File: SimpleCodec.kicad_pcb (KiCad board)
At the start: 4 copper layers, 115 parts, among them J1 DC-005-2.5A-2.0, J2 NMJ6HCD2, J3 NMJ6HCD2, Q1 AO3401A, U1 AMS1117-5.0, U2 AMS1117-3.3, U3 NE5532, U4 NE5532, U5 NE5532, U6 NE5532, U7 NE5532, U8 CS4272

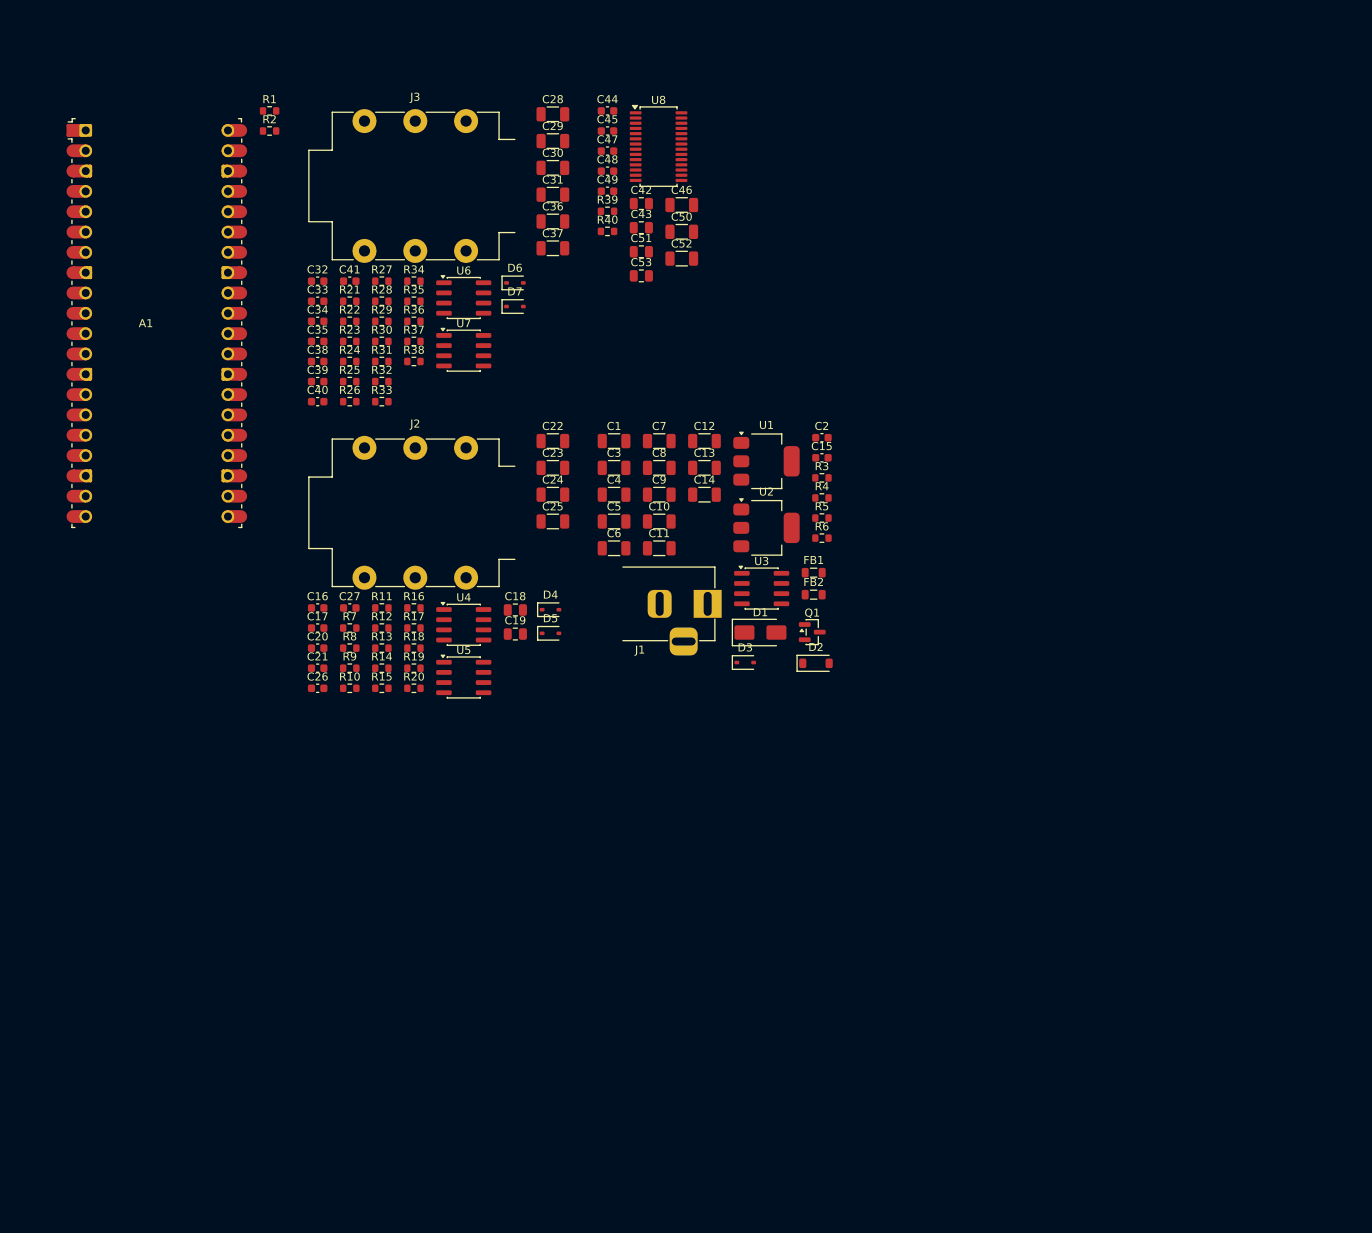
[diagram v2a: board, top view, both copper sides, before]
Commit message: Initial layout
Initial layout inside a 1590N1/125B pedal enclosure.
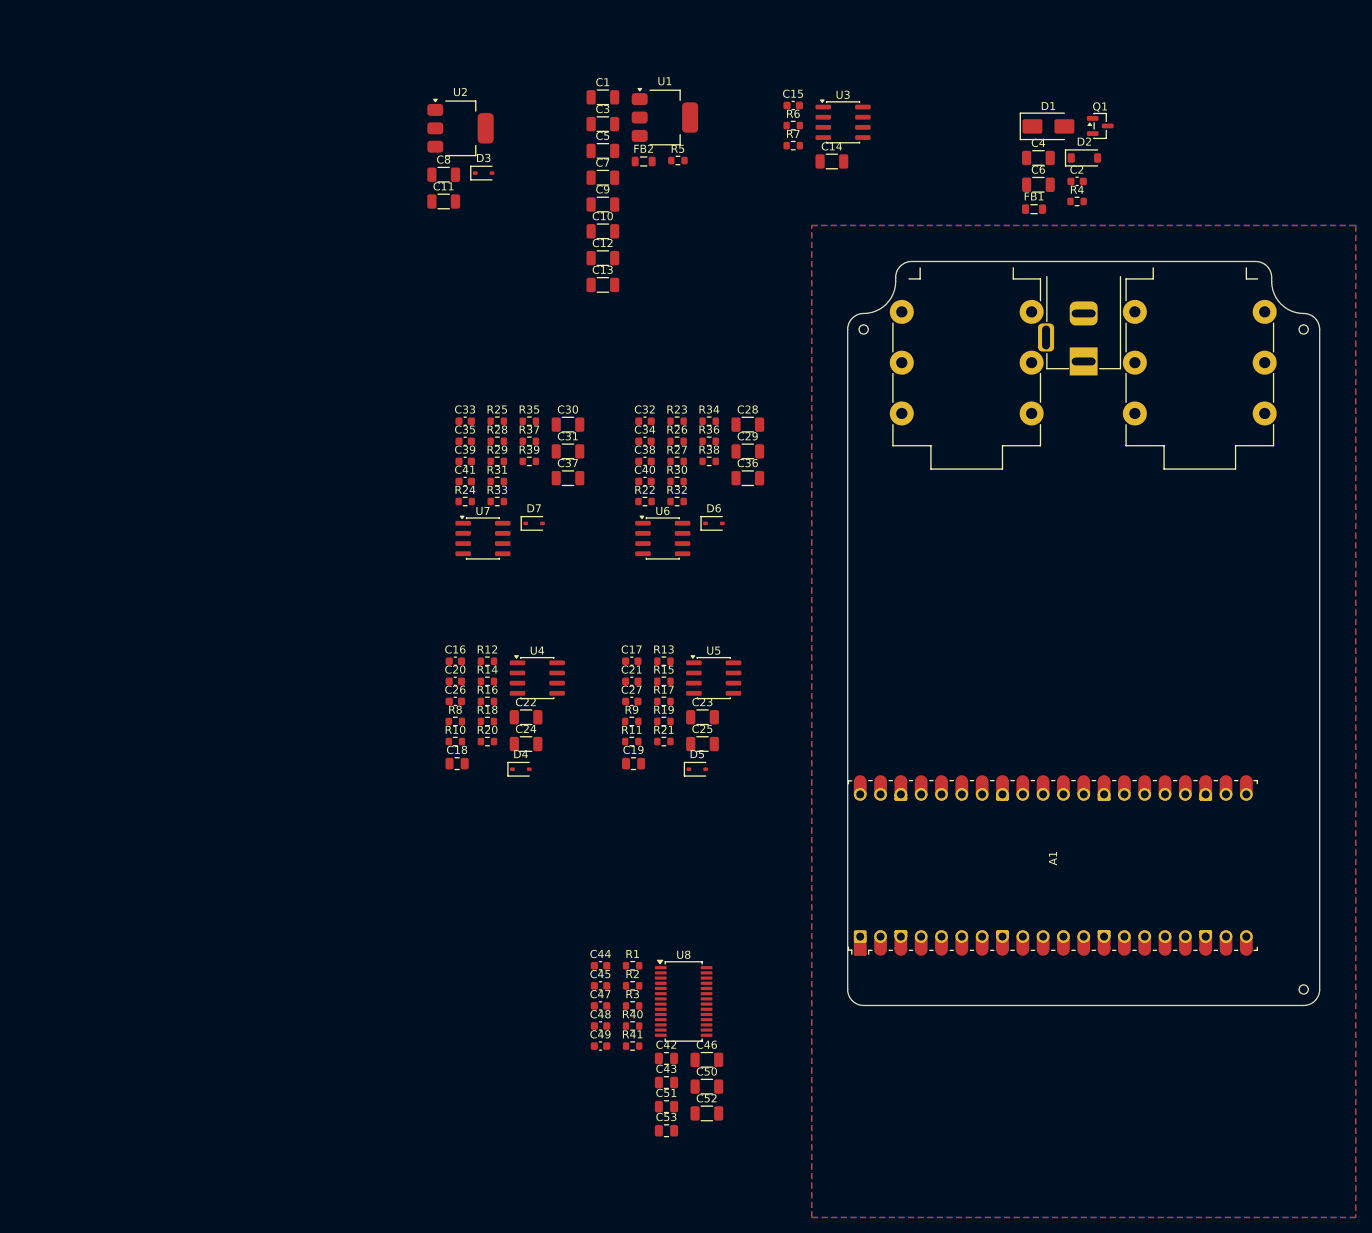
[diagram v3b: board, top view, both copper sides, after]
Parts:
- removed J1: DC-005-2.5A-2.0, Custom_Parts:BARREL_JACK_HORIZONTAL
- removed J2, J3: NMJ6HCD2, Custom_Parts:NMJ6HCD2_BORDER
- added H1: Tooling, MountingHole:ToolingHole_1.152mm, F.Cu at (122.5, 51.0)
- added H2: Tooling, MountingHole:ToolingHole_1.152mm, F.Cu at (177.5, 51.0)
- added H3: Tooling, MountingHole:ToolingHole_1.152mm, F.Cu at (177.5, 133.5)
- added R41: 47K, Resistor_SMD:R_0603_1608Metric, F.Cu at (93.6, 140.6)
- added REF**: Hammond_125B_1590N1_NOLID, Enclosures:Hammond_125B_1590N1_NOLID, B.Cu at (150.0, 100.0)
- added X1: PEDAL_COMBO_TOP, Custom_Parts:PEDAL_COMBO_TOP, F.Cu at (150.0, 44.0)
- R13: value 1K -> 100K
- R17: value 10K -> 1K
- R19: value 1K -> 10K
- R21: value 100K -> 1K
- R25: value 12K -> 100K
- R29: value 22K -> 12K
- R3: value 4.7K -> 47K
- R33: value 220 -> 22K
- R35: value 100 -> 220
- R37: value 47K -> 100
- R4, R7: value 100 -> 4.7K
- R5: value 4.7K -> 100
- R9: value 100K -> 100
- moved A1 130.9 mm to (146.2, 118.0), turned to 90 degrees
- moved R1 116.1 mm to (93.6, 130.5)
- moved R2 116.1 mm to (93.6, 133.0)
- moved C50 106.9 mm to (102.9, 145.6)
- moved C51 106.9 mm to (97.8, 148.1)
- moved C52 106.9 mm to (102.9, 149.0)
- moved C53 106.9 mm to (97.8, 151.2)
- moved U8 106.9 mm to (100.0, 135.0)
- moved C42 106.9 mm to (97.8, 142.1)
- moved C43 106.9 mm to (97.8, 145.1)
- moved C46 106.9 mm to (102.9, 142.3)
- moved C47 106.9 mm to (89.6, 135.6)
- moved C44 106.9 mm to (89.6, 130.5)
- moved C45 106.9 mm to (89.6, 133.0)
- moved C48 106.9 mm to (89.6, 138.1)
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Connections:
- R10 pad 2: Net-(C17-Pad1) -> Net-(C16-Pad1)
- R11 pad 1: Net-(U4A-+) -> GND
- R11 pad 2: +VBIAS_IN -> Net-(C17-Pad1)
- R12 pad 1: Net-(U5A-+) -> Net-(U4A-+)
- R13 pad 1: Net-(U4A--) -> Net-(U5A-+)
- R13 pad 2: Net-(C20-Pad1) -> +VBIAS_IN
- R14 pad 1: Net-(U5A--) -> Net-(U4A--)
- R14 pad 2: Net-(C21-Pad1) -> Net-(C20-Pad1)
- R15 pad 1: GND -> Net-(U5A--)
- R15 pad 2: Net-(C20-Pad1) -> Net-(C21-Pad1)
- R16 pad 2: Net-(C21-Pad1) -> Net-(C20-Pad1)
- R17 pad 1: Net-(U4B-+) -> GND
- R17 pad 2: VBIAS_IN -> Net-(C21-Pad1)
- R18 pad 1: Net-(U5B-+) -> Net-(U4B-+)
- R19 pad 1: Net-(C24-Pad2) -> Net-(U5B-+)
- R19 pad 2: CODEC_INL -> VBIAS_IN
- R20 pad 1: Net-(C25-Pad2) -> Net-(C24-Pad2)
- R20 pad 2: CODEC_INR -> CODEC_INL
- R21 pad 1: +VBIAS_OUT -> Net-(C25-Pad2)
- R21 pad 2: Net-(C28-Pad2) -> CODEC_INR
- R22 pad 1: Net-(C29-Pad2) -> +VBIAS_OUT
- R22 pad 2: VBIAS_OUT -> Net-(C28-Pad2)
- R23 pad 1: +VBIAS_OUT -> Net-(C29-Pad2)
- R23 pad 2: Net-(C30-Pad2) -> VBIAS_OUT
- R24 pad 1: Net-(C31-Pad2) -> +VBIAS_OUT
- R24 pad 2: VBIAS_OUT -> Net-(C30-Pad2)
- R25 pad 1: Net-(C28-Pad2) -> Net-(C31-Pad2)
- R25 pad 2: Net-(U6A--) -> VBIAS_OUT
- R26 pad 1: Net-(C29-Pad2) -> Net-(C28-Pad2)
- R26 pad 2: Net-(U6A-+) -> Net-(U6A--)
- R27 pad 1: Net-(C30-Pad2) -> Net-(C29-Pad2)
- R27 pad 2: Net-(U7A--) -> Net-(U6A-+)
- R28 pad 1: Net-(C31-Pad2) -> Net-(C30-Pad2)
- R28 pad 2: Net-(U7A-+) -> Net-(U7A--)
- R29 pad 1: Net-(U6A-+) -> Net-(C31-Pad2)
- R29 pad 2: VBIAS_OUT -> Net-(U7A-+)
- R3 pad 1: /Power/PROT_G -> CODEC_RST
- R30 pad 1: Net-(U7A-+) -> Net-(U6A-+)
- R31 pad 1: Net-(U6A--) -> Net-(U7A-+)
- R31 pad 2: Net-(C32-Pad2) -> VBIAS_OUT
- R32 pad 1: Net-(U7A--) -> Net-(U6A--)
- R32 pad 2: Net-(C33-Pad2) -> Net-(C32-Pad2)
- R33 pad 1: Net-(C32-Pad2) -> Net-(U7A--)
- R33 pad 2: Net-(U6B-+) -> Net-(C33-Pad2)
- R34 pad 1: Net-(C33-Pad2) -> Net-(C32-Pad2)
- R34 pad 2: Net-(U7B-+) -> Net-(U6B-+)
- R35 pad 1: Net-(C36-Pad2) -> Net-(C33-Pad2)
- R35 pad 2: /Buffers_Out/AUDIO_OUTL -> Net-(U7B-+)
- R36 pad 1: Net-(C37-Pad2) -> Net-(C36-Pad2)
- R36 pad 2: /Buffers_Out/AUDIO_OUTR -> /Buffers_Out/AUDIO_OUTL
- R37 pad 1: /Buffers_Out/AUDIO_OUTL -> Net-(C37-Pad2)
- R37 pad 2: GND -> /Buffers_Out/AUDIO_OUTR
- R38 pad 1: /Buffers_Out/AUDIO_OUTR -> /Buffers_Out/AUDIO_OUTL
- R39 pad 1: Net-(U8-~{BMUTEC}) -> /Buffers_Out/AUDIO_OUTR
- R4 pad 1: +VCC -> /Power/PROT_G
- R4 pad 2: +VCC_FILT -> GND
- R40 pad 1: Net-(U8-~{AMUTEC}) -> Net-(U8-~{BMUTEC})
- R5 pad 1: +VCC_FILT -> +VCC
- R5 pad 2: /Power/+VBIAS_RAW -> +VCC_FILT
- R6 pad 1: /Power/+VBIAS_RAW -> +VCC_FILT
- R6 pad 2: GND -> /Power/+VBIAS_RAW
- R7 pad 1: /Buffers_In/AUDIO_INL -> /Power/+VBIAS_RAW
- R7 pad 2: Net-(C16-Pad1) -> GND
- R8 pad 1: /Buffers_In/AUDIO_INR -> /Buffers_In/AUDIO_INL
- R8 pad 2: Net-(C17-Pad1) -> Net-(C16-Pad1)
- R9 pad 1: GND -> /Buffers_In/AUDIO_INR
- R9 pad 2: Net-(C16-Pad1) -> Net-(C17-Pad1)
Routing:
- added copper zone on B.Cu, net GND
- added copper zone on F.Cu, net GND
- added copper zone on In1.Cu, net GND
- added copper zone on In2.Cu, net GND
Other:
- board outline added: 59 x 93 mm

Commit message: RP2350 layout
Updated the layout for the RP2350.
Added board headers.
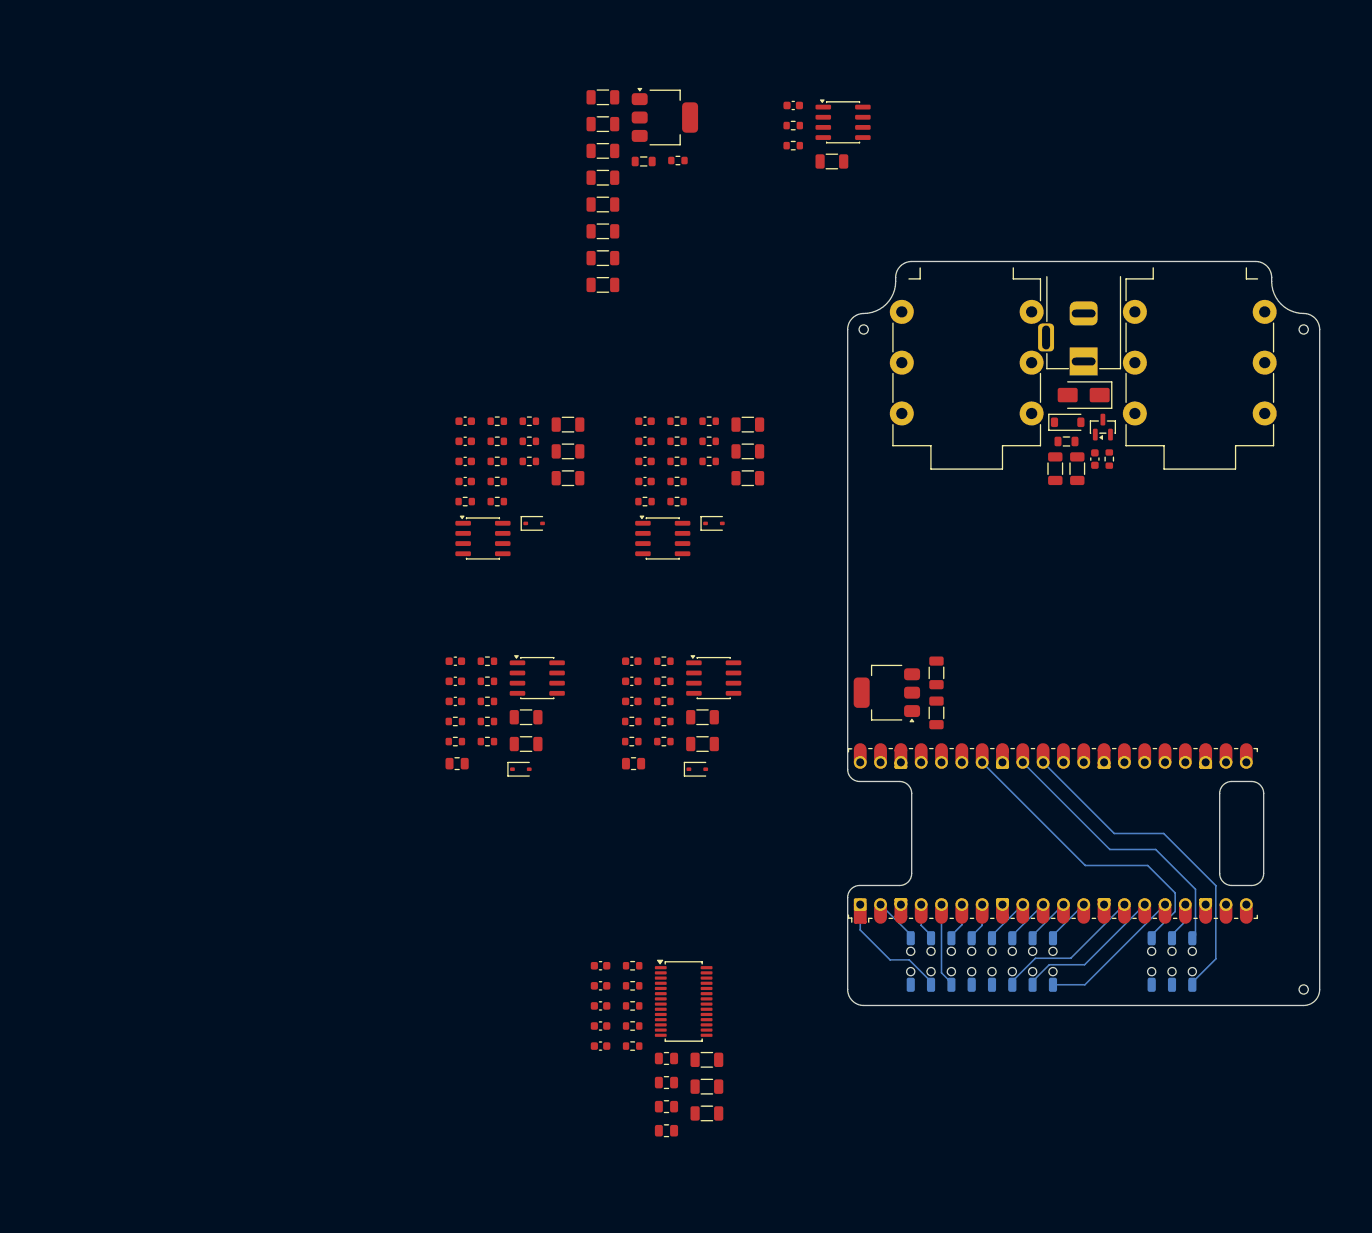
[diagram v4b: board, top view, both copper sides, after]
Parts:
- removed the D3 at (75.0, 31.4)
- removed the R1 at (93.6, 130.5)
- removed the R2 at (93.6, 133.0)
- added J1: RPI_ADC, Custom_Parts:HEADER_THROUGH_2x03_P2.54mm, B.Cu at (161.0, 130.0)
- added J2: RP_GPIO, Custom_Parts:HEADER_THROUGH_2x08_P2.54mm, B.Cu at (137.3, 130.0)
- added R38: 47K, Resistor_SMD:R_0603_1608Metric, F.Cu at (93.6, 133.0)
- added R39: 47K, Resistor_SMD:R_0603_1608Metric, F.Cu at (93.6, 135.6)
- moved C12 88.8 mm to (131.6, 98.9), turned to -90 degrees
- moved U2 88.4 mm to (125.4, 96.4), turned to 180 degrees
- moved C9 87.6 mm to (131.6, 93.9), turned to 90 degrees
- moved C4 39.1 mm to (149.2, 68.4), turned to -90 degrees
- moved Q1 37.6 mm to (152.4, 63.2), turned to 90 degrees
- moved C6 35.6 mm to (146.4, 68.4), turned to -90 degrees
- moved C2 34.8 mm to (151.4, 67.2), turned to -90 degrees
- moved D1 33.9 mm to (150.0, 59.2), turned to 180 degrees
- moved D2 33.1 mm to (148.0, 62.6)
- moved R2 32.5 mm to (153.2, 67.2), turned to -90 degrees
- moved FB1 29.3 mm to (147.8, 65.0), turned to 180 degrees
- moved R1 5.02 mm to (93.6, 130.5)
- moved A1 4.00 mm to (146.2, 114.0)
- renumbered C12 to C11, C11 to C12, C9 to C8, C8 to C9, D4 to D3, D5 to D4, D6 to D5, D7 to D6, R3 to R1, R12 to R10, R13 to R11, R14 to R12, R15 to R13, R16 to R14, R17 to R15, R18 to R16, R19 to R17, R20 to R18, R21 to R19, R4 to R2, R22 to R20, R23 to R21, R24 to R22, R25 to R23, R26 to R24, R27 to R25, R28 to R26, R29 to R27, R30 to R28, R31 to R29, R5 to R3, R32 to R30, R33 to R31, R34 to R32, R35 to R33, R36 to R34, R37 to R35, R38 to R36, R39 to R37, R6 to R4, R7 to R5, R8 to R6, R9 to R7, R10 to R8, R11 to R9
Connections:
- net Net-(U8-~{AMUTEC}) renamed /Codec/AMUTEC
- net Net-(U8-~{BMUTEC}) renamed /Codec/BMUTEC
- A1 pad 1: unconnected-(A1-GPIO0-Pad1) -> /GPIO0
- A1 pad 10: unconnected-(A1-GPIO7-Pad10)_1 -> /GPIO7
- A1 pad 11: unconnected-(A1-GPIO8-Pad11) -> /GPIO8
- A1 pad 12: unconnected-(A1-GPIO9-Pad12)_1 -> /GPIO9
- A1 pad 14: unconnected-(A1-GPIO10-Pad14)_1 -> /GPIO10
- A1 pad 15: unconnected-(A1-GPIO11-Pad15) -> /GPIO11
- A1 pad 16: I2C_SDA -> /GPIO12
- A1 pad 17: I2C_SCL -> /GPIO13
- A1 pad 19: unconnected-(A1-GPIO14-Pad19)_1 -> I2C_SDA
- A1 pad 2: unconnected-(A1-GPIO1-Pad2)_1 -> /GPIO1
- A1 pad 20: unconnected-(A1-GPIO15-Pad20)_1 -> I2C_SCL
- A1 pad 27: unconnected-(A1-GPIO21-Pad27) -> CODEC_RST
- A1 pad 29: CODEC_RST -> unconnected-(A1-GPIO22-Pad29)_1
- A1 pad 31: unconnected-(A1-GPIO26_ADC0-Pad31) -> /ADC0
- A1 pad 32: unconnected-(A1-GPIO27_ADC1-Pad32)_1 -> /ADC1
- A1 pad 33: unconnected-(A1-AGND-Pad33)_1 -> GND
- A1 pad 34: unconnected-(A1-GPIO28_ADC2-Pad34) -> /ADC2
- A1 pad 35: unconnected-(A1-ADC_VREF-Pad35) -> +3V3D
- A1 pad 36: unconnected-(A1-3V3-Pad36) -> +3V3D
- A1 pad 37: unconnected-(A1-3V3_EN-Pad37)_1 -> GND
- A1 pad 39: +VSYS -> unconnected-(A1-VSYS-Pad39)
- A1 pad 4: unconnected-(A1-GPIO2-Pad4) -> /GPIO2
- A1 pad 5: unconnected-(A1-GPIO3-Pad5)_1 -> /GPIO3
- A1 pad 6: unconnected-(A1-GPIO4-Pad6)_1 -> /GPIO4
- A1 pad 7: unconnected-(A1-GPIO5-Pad7)_1 -> /GPIO5
- A1 pad 9: unconnected-(A1-GPIO6-Pad9) -> /GPIO6
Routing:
- net /ADC0: track 0.00 -> 41.6 mm
- net /ADC2: track 0.00 -> 37.8 mm
- net /ADC1: track 0.00 -> 34.4 mm
- net /GPIO11: track 0.00 -> 18.4 mm
- net /GPIO10: track 0.00 -> 18.4 mm
- net /GPIO12: track 0.00 -> 18.2 mm
- net /GPIO0: track 0.00 -> 15.1 mm
- net /GPIO3: track 0.00 -> 10.5 mm
- net /GPIO9: track 0.00 -> 5.79 mm
- net /GPIO8: track 0.00 -> 5.79 mm
- net /GPIO7: track 0.00 -> 5.79 mm
- net /GPIO6: track 0.00 -> 5.79 mm
- net /GPIO1: track 0.00 -> 5.76 mm
- net /GPIO13: track 0.00 -> 4.89 mm
- net /GPIO4: track 0.00 -> 4.74 mm
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- removed copper zone on B.Cu, net GND
- removed copper zone on F.Cu, net GND
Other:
- outline, holes or cut-outs redrawn
